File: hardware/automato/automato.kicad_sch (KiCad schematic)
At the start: 86 parts, among them J1 Motor1, J10 Servo 3, J11 Servo 4, J12 Barrel_Jack, J2 Motor2, J3 Motor4, J4 Motor3, J5 Servo 1, J6 i2c, J7 Servo 2, J8 Relay 1, J9 Relay 2, K1 G5Q-1A, K2 G5Q-1A, Q1 AO3400A, Q2 AO3400A, Q3 AO3400A, Q4 AO3400A, Q5 AO3400A, Q6 AO3400A, Q7 HY12P03C2, U1 ESP32-C6-DEVKITC-1-N8, U6 TPS5450DDAR

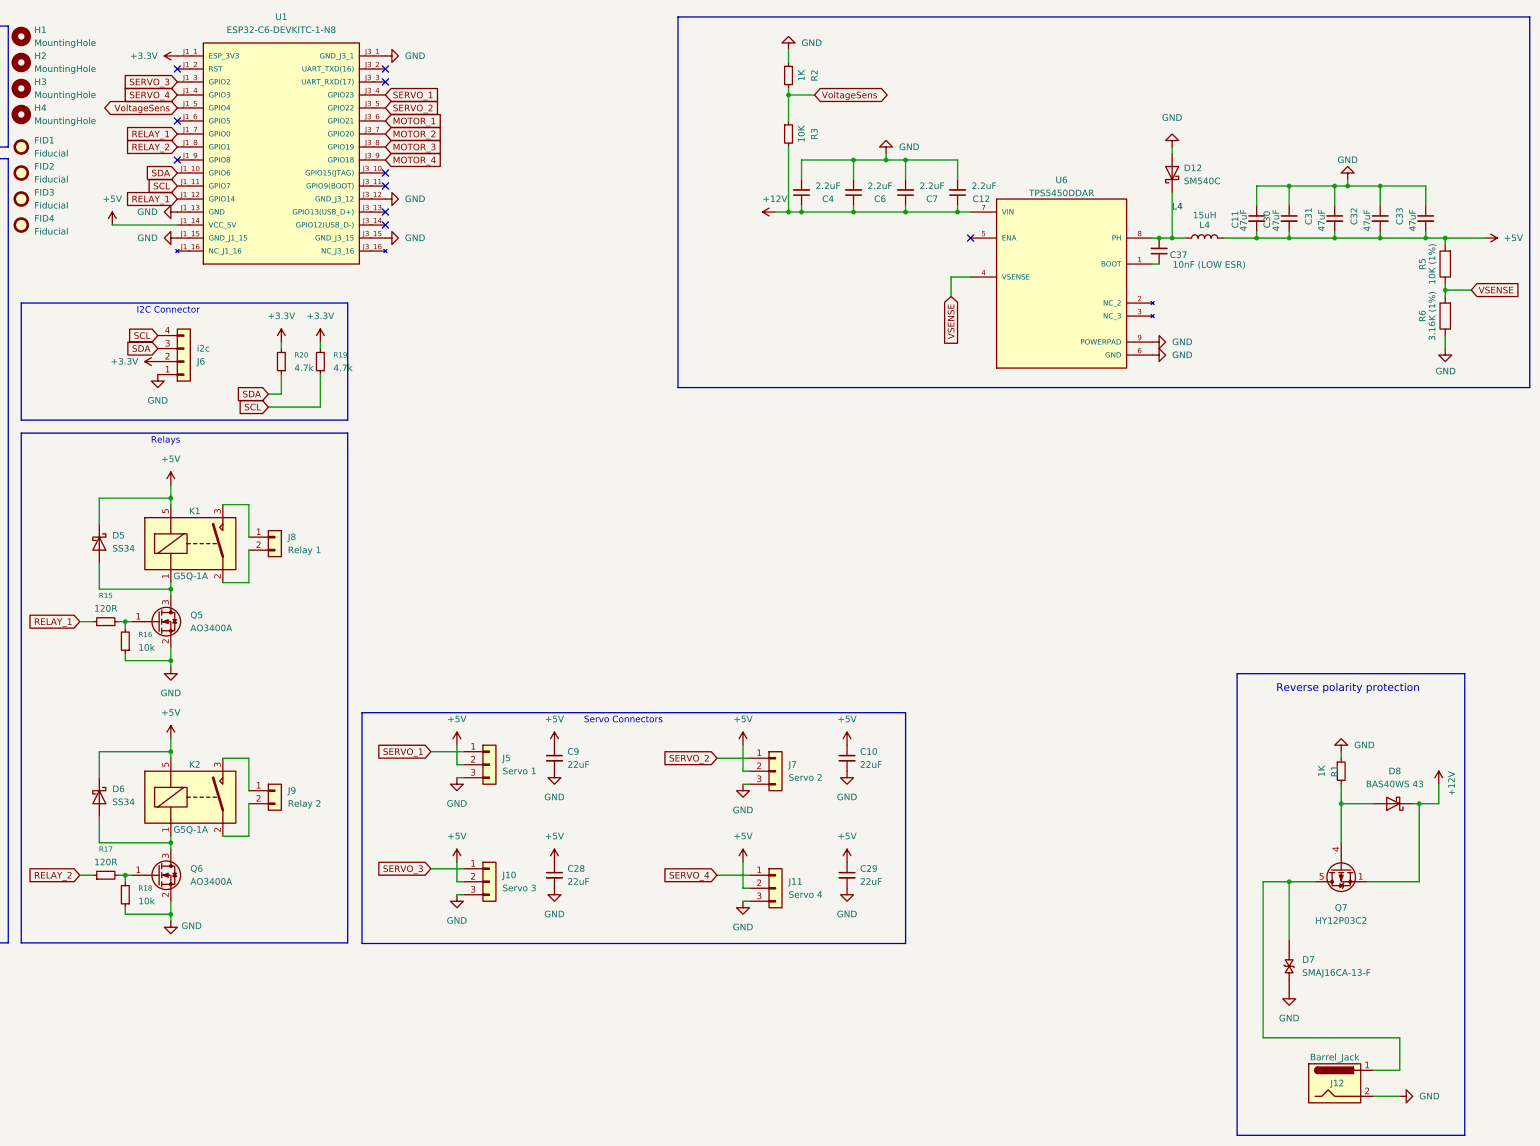
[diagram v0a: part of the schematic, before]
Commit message: sent to production
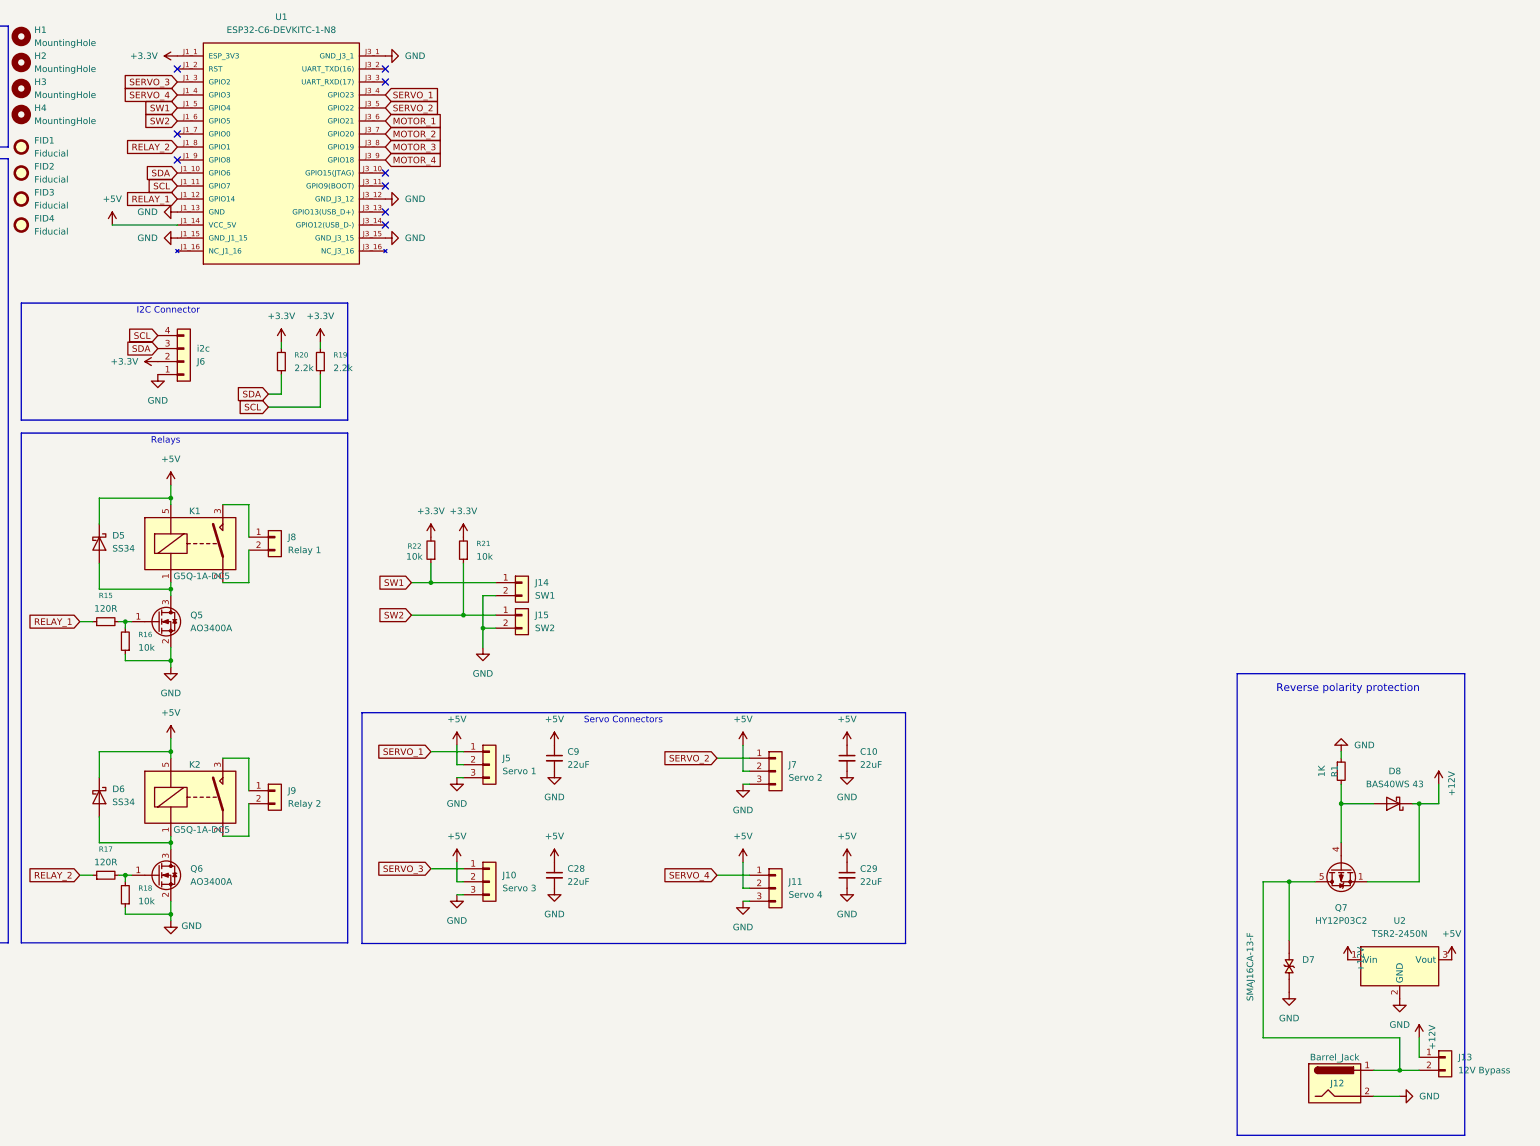
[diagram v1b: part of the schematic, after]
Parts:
- removed C11, C30, C31, C32, C33: 47uF, Capacitor_SMD:C_0805_2012Metric, symbol Device:C_Small
- removed C12, C4, C6, C7: 2.2uF, Capacitor_SMD:C_0805_2012Metric, symbol Device:C_Small
- removed C37: 10nF (LOW ESR), Capacitor_SMD:C_0402_1005Metric, symbol Device:C_Small
- removed D12: SM540C, Diode_SMD:D_SMC, symbol Device:D_Schottky
- removed L4: 15uH, BlackPanda:L_10.5x11.5_H4.0, symbol Device:L
- removed R2: 1K, Resistor_SMD:R_0402_1005Metric, symbol Device:R_Small
- removed R3: 10K, Resistor_SMD:R_0402_1005Metric, symbol Device:R_Small
- removed R5: 10K (1%), Resistor_SMD:R_0402_1005Metric, symbol Device:R
- removed R6: 3.16K (1%), Capacitor_SMD:C_0603_1608Metric, symbol Device:R
- removed U6: TPS5450DDAR, BlackPanda:CONV_TPS5450DDAR, symbol TPS5450DDAR:TPS5450DDAR
- added J13: 12V Bypass, Connector_PinHeader_2.54mm:PinHeader_1x02_P2.54mm_Vertical, symbol Connector_Generic:Conn_01x02
- added J14: SW1, TerminalBlock_Phoenix:TerminalBlock_Phoenix_MKDS-1,5-2-5.08_1x02_P5.08mm_Horizontal, symbol Connector_Generic:Conn_01x02
- added J15: SW2, TerminalBlock_Phoenix:TerminalBlock_Phoenix_MKDS-1,5-2-5.08_1x02_P5.08mm_Horizontal, symbol Connector_Generic:Conn_01x02
- added R21, R22: 10k, Resistor_SMD:R_0603_1608Metric, symbol Device:R_Small
- added U2: TSR2-2450N, Converter_DCDC:Converter_DCDC_TRACO_TSR2-24xxN_TSR2-24xxxN_THT, symbol Converter_DCDC:TSR2-2450N
- C16: LCSC (none) -> C602037
- D1: LCSC (none) -> C908680
- D7: PartNr (none) -> C134960
- D8: PartNr (none) -> C22648
- J1: LCSC (none) -> C474900
- J12: PartNr (none) -> C720557
- K1, K2: value G5Q-1A -> G5Q-1A-DC5; PartNr (none) -> 653-G5Q-1A-DC5
- Q1: LCSC (none) -> C20917
- Q7: PartNr (none) -> C358006
- R1: footprint Resistor_SMD:R_0402_1005Metric -> Capacitor_SMD:C_0603_1608Metric
- R19, R20: value 4.7k -> 2.2k
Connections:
- net +12V: now also J13.1 (Pin_1), U2.1 (Vin)
- net +3.3V: now also R21.2, R22.2
- net +5V: now also U2.3 (Vout)
- net GND: now also J14.2 (Pin_2), J15.2 (Pin_2), U2.2 (GND)
- net RELAY_1: no longer U1.J1_7 (GPIO0)
- net SW2: now reaches U1.J1_6 (GPIO5)
- net SW2: now also J15.1 (Pin_1), R21.1
- net at D7.2, J12.1, Q7.5 (D): now also J13.2 (Pin_2)
- net VoltageSens renamed SW1
- net SW1: now also J14.1 (Pin_1), R22.1
- no-connect marks 10 -> 9
